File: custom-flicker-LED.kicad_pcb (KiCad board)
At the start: 2 copper layers, 5.4 x 5.8 mm, 10 parts, among them J1 Conn_01x01, J2 Conn_01x01, J3 TPI interface, Q1 MMBT3904M, U1 ATtiny20-UU, U2 TCR3UG18A

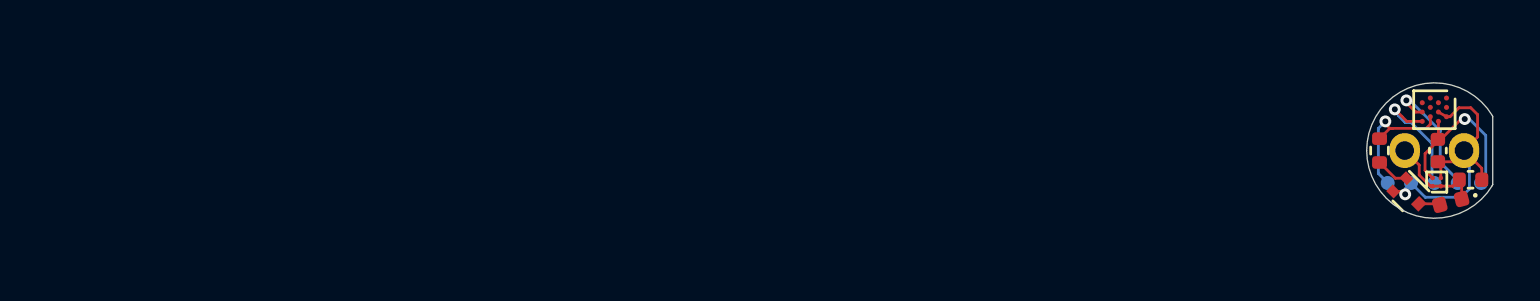
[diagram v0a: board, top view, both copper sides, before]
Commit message: Migrated to KiCad 6 and a much better circuit
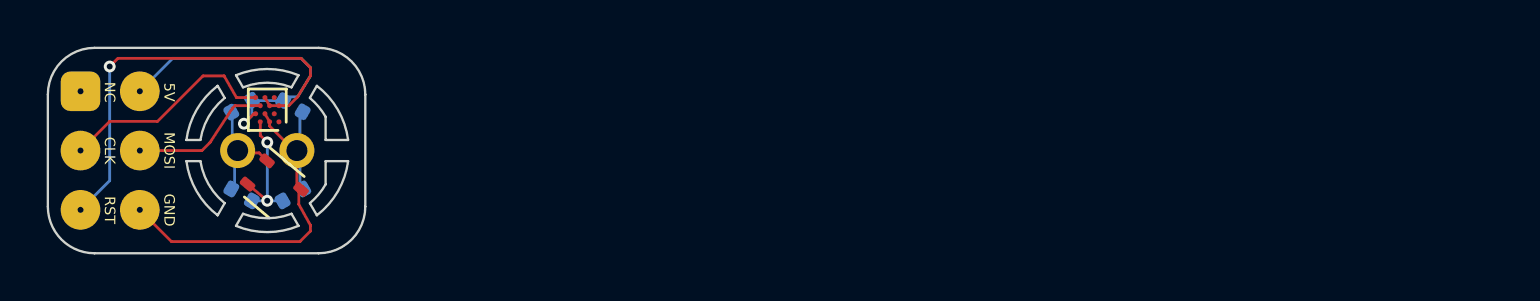
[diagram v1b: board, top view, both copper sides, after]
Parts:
- removed C2: 1μF, Capacitor_SMD:C_0402_1005Metric
- removed D2: CZRQR52C2-HF, Diode_SMD:D_0402_1005Metric
- removed J2: Conn_01x01, Connector_PinSocket_2.54mm:PinSocket_1x01_P2.54mm_Vertical
- removed J3: TPI interface, custom-flicker-LED:padz
- removed Q1: MMBT3904M, Package_TO_SOT_SMD:SOT-723
- added D1: LED_big, LED_THT:LED_D5.0mm_Clear, B.Cu at (100.0, 100.0)
- added R1: 1kΩ, Resistor_SMD:R_0402_1005Metric, B.Cu at (98.9, 98.1)
- added R3: 7.5kΩ, Resistor_SMD:R_0402_1005Metric, B.Cu at (101.1, 101.9)
- C1: value 1μF -> 0.1μF; moved to B.Cu
- J1: value Conn_01x01 -> TPI Interface; footprint Connector_PinSocket_2.54mm:PinSocket_1x01_P2.54mm_Vertical -> Connector_PinHeader_2.54mm:PinHeader_2x03_P2.54mm_Vertical; moved to F.Cu
- R2: value 1kΩ -> 4.5kΩ; moved to B.Cu
- U2: value TCR3UG18A -> TL431DCK; footprint custom-flicker-LED:WCSP-4F_0.65x0.65mm_P0.35mm -> Package_TO_SOT_SMD:SOT-363_SC-70-6
- moved J1 56.8 mm to (92.0, 97.5)
- moved U1 50.0 mm to (100.0, 98.2), turned to 180 degrees
- moved U2 49.8 mm to (100.3, 101.5), turned to -40 degrees
- moved C1 49.1 mm to (101.1, 98.1), turned to 150 degrees
- moved R2 48.8 mm to (98.9, 101.9), turned to 150 degrees
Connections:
- C1 pad 1: GNDREF -> /LED-
- C1 pad 2: /1.8V -> /V_{cc}
- J1 pad 1: /LED+ -> unconnected-(J1-Pad1)
- R2 pad 1: Net-(Q1-Pad1) -> Net-(R2-Pad1)
- R2 pad 2: /mosi -> /LED+
- U1 pad A1: Net-(U1-PadA1) -> unconnected-(U1-PadA1)
- U1 pad A3: Net-(U1-PadA3) -> /LED-
- U1 pad A5: GNDREF -> Net-(R2-Pad1)
- U1 pad B2: Net-(U1-PadB2) -> unconnected-(U1-PadB2)
- U1 pad B4: GNDREF -> /LED-
- U1 pad B6: /1.8V -> /V_{cc}
- U1 pad C1: Net-(U1-PadC1) -> /rst
- U1 pad C3: Net-(U1-PadC3) -> /rst
- U1 pad D2: Net-(U1-PadD2) -> unconnected-(U1-PadD2)
- U1 pad D4: /~rst -> /rst
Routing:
- net /rst: track 0.00 -> 18.7 mm, vias 0 -> 1
- net /LED-: track 0.00 -> 17.5 mm
- net /V_{cc}: track 0.00 -> 13.3 mm, vias 0 -> 1
- net GNDREF: track 13.3 -> 0.00 mm, vias 1 -> 0
- net /1.8V: track 7.62 -> 0.00 mm, vias 1 -> 0
- net Net-(R2-Pad1): track 0.00 -> 5.93 mm, vias 0 -> 2
- net /~rst: track 5.49 -> 0.00 mm, vias 1 -> 0
- net /clk: track 5.39 -> 9.37 mm, vias 1 -> 0
- net Net-(Q1-Pad1): track 1.43 -> 0.00 mm
- net Net-(D2-Pad2): track 0.92 -> 0.00 mm
- net /LED+: track 4.10 -> 4.98 mm
- net /mosi: track 6.07 -> 6.14 mm, vias 1 -> 0
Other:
- board size 5.4 x 5.8 mm -> 13.6 x 8.8 mm
- net class Default removed
- board text added: "5V"
- board text added: "CLK"
- board text added: "Fluoro LED v6r4"
- board text added: "GND"
- board text added: "January 2022"
- board text added: "MOSI"
- board text added: "NC"
- board text added: "RST"

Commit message: Update to show it working IRL, wooooo
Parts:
- R2: value 4.5kΩ -> 4.7kΩ
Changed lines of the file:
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@@
     (descr "Through hole straight pin header, 2x03, 2.54mm pitch, double rows")
     (tags "Through hole pin header THT 2x03 2.54mm double row")
-    (property "Sheetfile" "fluoro_LED.kicad_sch")
+    (property "Sheetfile" "custom-flicker-LED.kicad_sch")
     (property "Sheetname" "")
     (attr through_hole)
@@
     (descr "SOT-363, SC-70-6")
     (tags "SOT-363 SC-70-6")
-    (property "Sheetfile" "fluoro_LED.kicad_sch")
+    (property "Sheetfile" "custom-flicker-LED.kicad_sch")
     (property "Sheetname" "")
     (attr smd)
@@
     (descr "WLCSP-12, 6x4 raster staggered array, 1.403x1.555mm package, pitch 0.4mm; http://ww1.microchip.com/downloads/en/devicedoc/atmel-8235-8-bit-avr-microcontroller-attiny20_datasheet.pdf#page=208")
     (tags "CSP 12 0.2x0.346333")
-    (property "Sheetfile" "fluoro_LED.kicad_sch")
+    (property "Sheetfile" "custom-flicker-LED.kicad_sch")
     (property "Sheetname" "")
     (solder_mask_margin 0.0325)
@@
     (descr "LED, diameter 5.0mm, 2 pins, http://cdn-reichelt.de/documents/datenblatt/A500/LL-504BC2E-009.pdf")
     (tags "LED diameter 5.0mm 2 pins")
-    (property "Sheetfile" "fluoro_LED.kicad_sch")
+    (property "Sheetfile" "custom-flicker-LED.kicad_sch")
     (property "Sheetname" "")
     (attr through_hole)
@@
     (descr "Resistor SMD 0402 (1005 Metric), square (rectangular) end terminal, IPC_7351 nominal, (Body size source: IPC-SM-782 page 72, https://www.pcb-3d.com/wordpress/wp-content/uploads/ipc-sm-782a_amendment_1_and_2.pdf), generated with kicad-footprint-generator")
     (tags "resistor")
-    (property "Sheetfile" "fluoro_LED.kicad_sch")
+    (property "Sheetfile" "custom-flicker-LED.kicad_sch")
     (property "Sheetname" "")
     (attr smd)
@@
     (descr "Resistor SMD 0402 (1005 Metric), square (rectangular) end terminal, IPC_7351 nominal, (Body size source: IPC-SM-782 page 72, https://www.pcb-3d.com/wordpress/wp-content/uploads/ipc-sm-782a_amendment_1_and_2.pdf), generated with kicad-footprint-generator")
     (tags "resistor")
-    (property "Sheetfile" "fluoro_LED.kicad_sch")
+    (property "Sheetfile" "custom-flicker-LED.kicad_sch")
     (property "Sheetname" "")
     (attr smd)
@@
     (descr "Capacitor SMD 0402 (1005 Metric), square (rectangular) end terminal, IPC_7351 nominal, (Body size source: IPC-SM-782 page 76, https://www.pcb-3d.com/wordpress/wp-content/uploads/ipc-sm-782a_amendment_1_and_2.pdf), generated with kicad-footprint-generator")
     (tags "capacitor")
-    (property "Sheetfile" "fluoro_LED.kicad_sch")
+    (property "Sheetfile" "custom-flicker-LED.kicad_sch")
     (property "Sheetname" "")
     (attr smd)
@@
     (descr "Resistor SMD 0402 (1005 Metric), square (rectangular) end terminal, IPC_7351 nominal, (Body size source: IPC-SM-782 page 72, https://www.pcb-3d.com/wordpress/wp-content/uploads/ipc-sm-782a_amendment_1_and_2.pdf), generated with kicad-footprint-generator")
     (tags "resistor")
-    (property "Sheetfile" "fluoro_LED.kicad_sch")
+    (property "Sheetfile" "custom-flicker-LED.kicad_sch")
     (property "Sheetname" "")
     (attr smd)
@@
       (effects (font (size 1 1) (thickness 0.15)) (justify mirror))
     )
-    (fp_text value "4.5kΩ" (at 0 -1.17 150) (layer "B.Fab") hide
-      (effects (font (size 1 1) (thickness 0.15)) (justify mirror))
-    )
+    (fp_text value "4.7kΩ" (at 0 -1.17 150) (layer "B.Fab") hide
+      (effects (font (size 1 1) (thickness 0.15)) (justify mirror))
+    )
